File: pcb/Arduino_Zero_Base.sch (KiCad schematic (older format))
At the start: 14 parts, among them U4 SAMD21G18A-A, Y1 32.768kHz

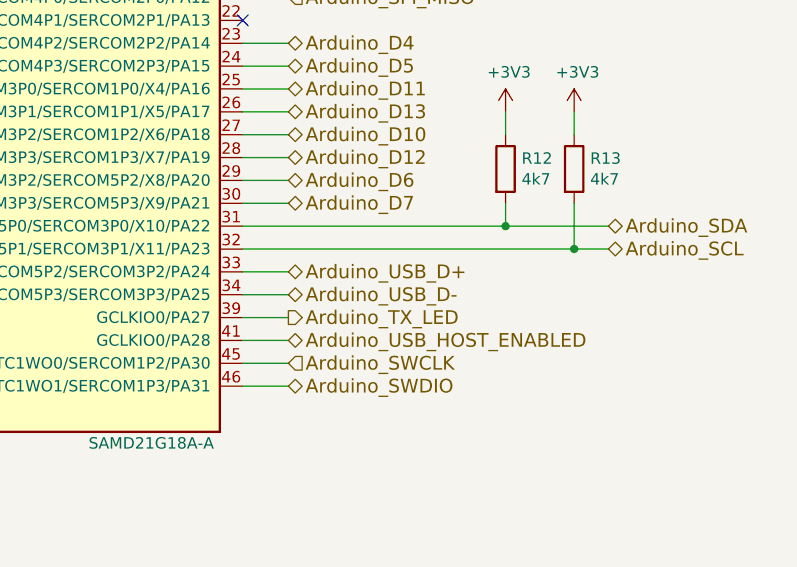
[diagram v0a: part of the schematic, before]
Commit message: Improve pcb routing, add testpoints and etc. The design improves a lot. Still lots to do, but most important design parts should now be drafted almost complete.
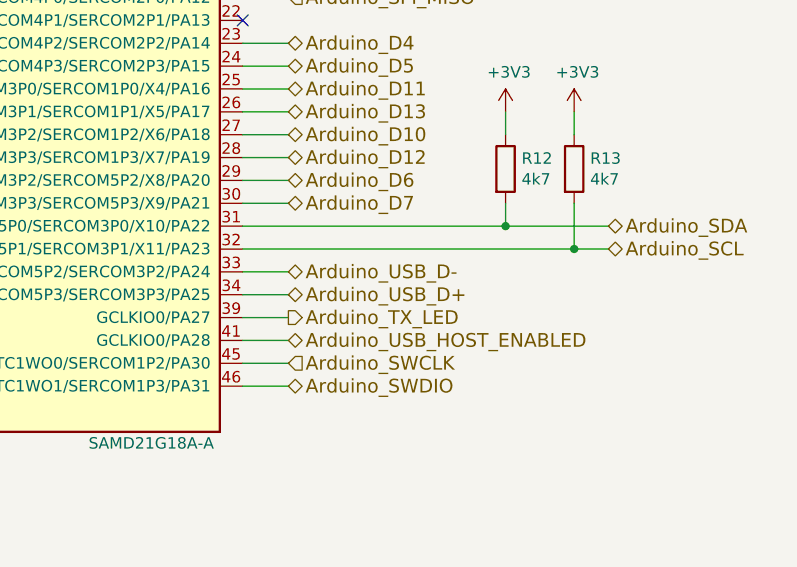
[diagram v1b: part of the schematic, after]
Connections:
- net Arduino_USB_D+: now also U4.34 (USBDP/TC5WO1/SERCOM5P3/SERCOM3P3/PA25); no longer U4.33 (USBDM/TC5WO0/SERCOM5P2/SERCOM3P2/PA24)
- net Arduino_USB_D-: now also U4.33 (USBDM/TC5WO0/SERCOM5P2/SERCOM3P2/PA24); no longer U4.34 (USBDP/TC5WO1/SERCOM5P3/SERCOM3P3/PA25)
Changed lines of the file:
@@
 $EndDescr
 $Comp
-L GND #PWR036
+L GND #PWR045
 U 1 1 5802079F
 P 8800 3350
-F 0 "#PWR036" H 8800 3100 50  0001 C CNN
+F 0 "#PWR045" H 8800 3100 50  0001 C CNN
 F 1 "GND" H 8805 3177 50  0000 C CNN
 F 2 "" H 8800 3350 50  0000 C CNN
@@
 $EndComp
 $Comp
-L GND #PWR037
+L GND #PWR046
 U 1 1 580207D5
 P 9200 3350
-F 0 "#PWR037" H 9200 3100 50  0001 C CNN
+F 0 "#PWR046" H 9200 3100 50  0001 C CNN
 F 1 "GND" H 9205 3177 50  0000 C CNN
 F 2 "" H 9200 3350 50  0000 C CNN
@@
 Connection ~ 8800 2950
 $Comp
-L GND #PWR038
+L GND #PWR047
 U 1 1 58028479
 P 5350 6050
-F 0 "#PWR038" H 5350 5800 50  0001 C CNN
+F 0 "#PWR047" H 5350 5800 50  0001 C CNN
 F 1 "GND" H 5355 5877 50  0000 C CNN
 F 2 "" H 5350 6050 50  0000 C CNN
@@
 $EndComp
 $Comp
-L GND #PWR039
+L GND #PWR048
 U 1 1 5802867C
 P 4950 6050
-F 0 "#PWR039" H 4950 5800 50  0001 C CNN
+F 0 "#PWR048" H 4950 5800 50  0001 C CNN
 F 1 "GND" H 4955 5877 50  0000 C CNN
 F 2 "" H 4950 6050 50  0000 C CNN
@@
 	5250 5950 5250 5850
 $Comp
-L +3V3 #PWR040
+L +3V3 #PWR049
 U 1 1 580289B7
 P 4600 1600
-F 0 "#PWR040" H 4600 1450 50  0001 C CNN
+F 0 "#PWR049" H 4600 1450 50  0001 C CNN
 F 1 "+3V3" H 4615 1773 50  0000 C CNN
 F 2 "" H 4600 1600 50  0000 C CNN
@@
 $EndComp
 $Comp
-L +3V3 #PWR041
+L +3V3 #PWR050
 U 1 1 58028A51
 P 5350 2250
-F 0 "#PWR041" H 5350 2100 50  0001 C CNN
+F 0 "#PWR050" H 5350 2100 50  0001 C CNN
 F 1 "+3V3" H 5365 2423 50  0000 C CNN
 F 2 "" H 5350 2250 50  0000 C CNN
@@
 $EndComp
 $Comp
-L GND #PWR042
+L GND #PWR051
 U 1 1 58028EFC
 P 5550 1950
-F 0 "#PWR042" H 5550 1700 50  0001 C CNN
+F 0 "#PWR051" H 5550 1700 50  0001 C CNN
 F 1 "GND" H 5555 1777 50  0000 C CNN
 F 2 "" H 5550 1950 50  0000 C CNN
@@
 $EndComp
 $Comp
-L GND #PWR043
+L GND #PWR052
 U 1 1 580295A1
 P 4600 2300
-F 0 "#PWR043" H 4600 2050 50  0001 C CNN
+F 0 "#PWR052" H 4600 2050 50  0001 C CNN
 F 1 "GND" H 4605 2127 50  0000 C CNN
 F 2 "" H 4600 2300 50  0000 C CNN
@@
 $EndComp
 $Comp
-L GND #PWR044
+L GND #PWR053
 U 1 1 58029E20
 P 6150 2050
-F 0 "#PWR044" H 6150 1800 50  0001 C CNN
+F 0 "#PWR053" H 6150 1800 50  0001 C CNN
 F 1 "GND" H 6155 1877 50  0000 C CNN
 F 2 "" H 6150 2050 50  0000 C CNN
@@
 $EndComp
 $Comp
-L GND #PWR045
+L GND #PWR054
 U 1 1 58029E5B
 P 7050 2050
-F 0 "#PWR045" H 7050 1800 50  0001 C CNN
+F 0 "#PWR054" H 7050 1800 50  0001 C CNN
 F 1 "GND" H 7055 1877 50  0000 C CNN
 F 2 "" H 7050 2050 50  0000 C CNN
@@
 $EndComp
 $Comp
-L +3V3 #PWR046
+L +3V3 #PWR055
 U 1 1 58029EA6
 P 6150 1650
-F 0 "#PWR046" H 6150 1500 50  0001 C CNN
+F 0 "#PWR055" H 6150 1500 50  0001 C CNN
 F 1 "+3V3" H 6165 1823 50  0000 C CNN
 F 2 "" H 6150 1650 50  0000 C CNN
@@
 $EndComp
 $Comp
-L +3V3 #PWR047
+L +3V3 #PWR056
 U 1 1 58029EE1
 P 7050 1650
-F 0 "#PWR047" H 7050 1500 50  0001 C CNN
+F 0 "#PWR056" H 7050 1500 50  0001 C CNN
 F 1 "+3V3" H 7065 1823 50  0000 C CNN
 F 2 "" H 7050 1650 50  0000 C CNN
@@
 	7450 5150 7650 5150
 Text HLabel 7650 5050 2    60   BiDi ~ 0
+Arduino_USB_D-
+Text HLabel 7650 5150 2    60   BiDi ~ 0
 Arduino_USB_D+
-Text HLabel 7650 5150 2    60   BiDi ~ 0
-Arduino_USB_D-
 Text HLabel 7650 3250 2    60   3State ~ 0
 Arduino_D8
@@
 $EndComp
 $Comp
-L +3V3 #PWR048
+L +3V3 #PWR057
 U 1 1 58034CF0
 P 8600 4350
-F 0 "#PWR048" H 8600 4200 50  0001 C CNN
+F 0 "#PWR057" H 8600 4200 50  0001 C CNN
 F 1 "+3V3" H 8615 4523 50  0000 C CNN
 F 2 "" H 8600 4350 50  0000 C CNN
@@
 $EndComp
 $Comp
-L +3V3 #PWR049
+L +3V3 #PWR058
 U 1 1 58034DB6
 P 8900 4350
-F 0 "#PWR049" H 8900 4200 50  0001 C CNN
+F 0 "#PWR058" H 8900 4200 50  0001 C CNN
 F 1 "+3V3" H 8915 4523 50  0000 C CNN
 F 2 "" H 8900 4350 50  0000 C CNN
@@
 $EndComp
 $Comp
-L GND #PWR050
+L GND #PWR059
 U 1 1 5803933E
 P 7550 2250
-F 0 "#PWR050" H 7550 2000 50  0001 C CNN
+F 0 "#PWR059" H 7550 2000 50  0001 C CNN
 F 1 "GND" H 7555 2077 50  0000 C CNN
 F 2 "" H 7550 2250 50  0000 C CNN
@@
 $EndComp
 $Comp
-L GND #PWR051
+L GND #PWR060
 U 1 1 5807F41A
 P 6600 2050
-F 0 "#PWR051" H 6600 1800 50  0001 C CNN
+F 0 "#PWR060" H 6600 1800 50  0001 C CNN
 F 1 "GND" H 6605 1877 50  0000 C CNN
 F 2 "" H 6600 2050 50  0000 C CNN
@@
 $EndComp
 $Comp
-L +3V3 #PWR052
+L +3V3 #PWR061
 U 1 1 5807F420
 P 6600 1650
-F 0 "#PWR052" H 6600 1500 50  0001 C CNN
+F 0 "#PWR061" H 6600 1500 50  0001 C CNN
 F 1 "+3V3" H 6615 1823 50  0000 C CNN
 F 2 "" H 6600 1650 50  0000 C CNN

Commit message: Add some digikey order informations to components
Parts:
- U4: Digi-Key Minimum Quantity (none) -> 1; Digi-Key Part Number (none) -> ATSAMD21G18A-AUTCT-ND
- Y1: Digi-Key Minimum Quantity (none) -> 1; Digi-Key Part Number (none) -> G83270022CT-ND
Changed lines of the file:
@@
 F 1 "SAMD21G18A-A" H 7050 2500 50  0000 C CNN
 F 2 "Housings_QFP:TQFP-48_7x7mm_Pitch0.5mm" H 5250 3000 50  0001 C CIN
-F 3 "" H 5250 4400 50  0000 C CNN
+F 3 "http://www.atmel.com/Images/Atmel-42181-SAM-D21_Datasheet.pdf" H 5250 4400 50  0001 C CNN
+F 4 "ATSAMD21G18A-AUTCT-ND" H 5250 4150 60  0001 C CNN "Digi-Key Part Number"
+F 5 "1" H 5250 4150 60  0001 C CNN "Digi-Key Minimum Quantity"
 	1    5250 4150
 	1    0    0    -1
@@
 F 1 "32.768kHz" H 9000 3084 50  0000 C CNN
 F 2 "Crystals:Crystal_SMD_G8" H 9000 2950 50  0001 C CNN
-F 3 "" H 9000 2950 50  0000 C CNN
+F 3 "https://media.digikey.com/pdf/Data%20Sheets/Pericom%20PDFs/G83270022_Ver.A.pdf" H 9000 2950 50  0001 C CNN
+F 4 "G83270022CT-ND" H 9000 2950 60  0001 C CNN "Digi-Key Part Number"
+F 5 "1" H 9000 2950 60  0001 C CNN "Digi-Key Minimum Quantity"
 	1    9000 2950
 	1    0    0    -1

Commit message: Add more BOM informations
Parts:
- C10, C11, C12, C13, C14, C9: Digi-Key Minimum Quantity (none) -> 1; Digi-Key Part Number (none) -> 311-1343-1-ND
- C15, C16: Digi-Key Minimum Quantity (none) -> 1; Digi-Key Part Number (none) -> 311-1062-1-ND
- R11: Digi-Key Minimum Quantity (none) -> 5000; Digi-Key Part Number (none) -> 311-330GRTR-ND
- R12, R13: Digi-Key Minimum Quantity (none) -> 5000; Digi-Key Part Number (none) -> 311-4.70KHRTR-ND
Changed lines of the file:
@@
 F 2 "Capacitors_SMD:C_0603" H 9200 3150 50  0001 C CNN
 F 3 "" H 9200 3150 50  0000 C CNN
+F 4 "311-1062-1-ND" H 9200 3150 60  0001 C CNN "Digi-Key Part Number"
+F 5 "1" H 9200 3150 60  0001 C CNN "Digi-Key Minimum Quantity"
 	1    9200 3150
 	-1   0    0    1
@@
 F 2 "Capacitors_SMD:C_0603" H 8800 3150 50  0001 C CNN
 F 3 "" H 8800 3150 50  0000 C CNN
+F 4 "311-1062-1-ND" H 8800 3150 60  0001 C CNN "Digi-Key Part Number"
+F 5 "1" H 8800 3150 60  0001 C CNN "Digi-Key Minimum Quantity"
 	1    8800 3150
 	-1   0    0    1
@@
 F 2 "Capacitors_SMD:C_0603" H 5550 2150 50  0001 C CNN
 F 3 "" H 5550 2150 50  0000 C CNN
+F 4 "311-1343-1-ND" H 5550 2150 60  0001 C CNN "Digi-Key Part Number"
+F 5 "1" H 5550 2150 60  0001 C CNN "Digi-Key Minimum Quantity"
 	1    5550 2150
 	-1   0    0    1
@@
 F 2 "Capacitors_SMD:C_0603" H 4600 2100 50  0001 C CNN
 F 3 "" H 4600 2100 50  0000 C CNN
+F 4 "311-1343-1-ND" H 4600 2100 60  0001 C CNN "Digi-Key Part Number"
+F 5 "1" H 4600 2100 60  0001 C CNN "Digi-Key Minimum Quantity"
 	1    4600 2100
 	-1   0    0    1
@@
 F 2 "Capacitors_SMD:C_0603" H 6150 1850 50  0001 C CNN
 F 3 "" H 6150 1850 50  0000 C CNN
+F 4 "311-1343-1-ND" H 6150 1850 60  0001 C CNN "Digi-Key Part Number"
+F 5 "1" H 6150 1850 60  0001 C CNN "Digi-Key Minimum Quantity"
 	1    6150 1850
 	-1   0    0    1
@@
 F 2 "Capacitors_SMD:C_0603" H 7050 1850 50  0001 C CNN
 F 3 "" H 7050 1850 50  0000 C CNN
+F 4 "311-1343-1-ND" H 7050 1850 60  0001 C CNN "Digi-Key Part Number"
+F 5 "1" H 7050 1850 60  0001 C CNN "Digi-Key Minimum Quantity"
 	1    7050 1850
 	-1   0    0    1
@@
 F 2 "Resistors_SMD:R_0603" V 2730 2650 50  0001 C CNN
 F 3 "" H 2800 2650 50  0000 C CNN
+F 4 "311-330GRTR-ND" H 2800 2650 60  0001 C CNN "Digi-Key Part Number"
+F 5 "5000" H 2800 2650 60  0001 C CNN "Digi-Key Minimum Quantity"
 	1    2800 2650
 	0    -1   -1   0
@@
 F 2 "Resistors_SMD:R_0603" V 8830 4600 50  0001 C CNN
 F 3 "" H 8900 4600 50  0000 C CNN
+F 4 "311-4.70KHRTR-ND" H 8900 4600 60  0001 C CNN "Digi-Key Part Number"
+F 5 "5000" H 8900 4600 60  0001 C CNN "Digi-Key Minimum Quantity"
 	1    8900 4600
 	1    0    0    -1
@@
 F 2 "Resistors_SMD:R_0603" V 8530 4600 50  0001 C CNN
 F 3 "" H 8600 4600 50  0000 C CNN
+F 4 "311-4.70KHRTR-ND" H 8600 4600 60  0001 C CNN "Digi-Key Part Number"
+F 5 "5000" H 8600 4600 60  0001 C CNN "Digi-Key Minimum Quantity"
 	1    8600 4600
 	1    0    0    -1
@@
 F 2 "Capacitors_SMD:C_0603" H 7550 2450 50  0001 C CNN
 F 3 "" H 7550 2450 50  0000 C CNN
+F 4 "311-1343-1-ND" H 7550 2450 60  0001 C CNN "Digi-Key Part Number"
+F 5 "1" H 7550 2450 60  0001 C CNN "Digi-Key Minimum Quantity"
 	1    7550 2450
 	-1   0    0    1
@@
 F 2 "Capacitors_SMD:C_0603" H 6600 1850 50  0001 C CNN
 F 3 "" H 6600 1850 50  0000 C CNN
+F 4 "311-1343-1-ND" H 6600 1850 60  0001 C CNN "Digi-Key Part Number"
+F 5 "1" H 6600 1850 60  0001 C CNN "Digi-Key Minimum Quantity"
 	1    6600 1850
 	-1   0    0    1

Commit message: Improve BOM
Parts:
- L1: value INDUCTOR_Small -> FERRIT_BEAD; Digi-Key Minimum Quantity (none) -> 1; Digi-Key Part Number (none) -> MH1608-471YCT-ND
- R11: Digi-Key Minimum Quantity 5000 -> 1; Digi-Key Part Number 311-330GRTR-ND -> 311-330GRCT-ND
- R12, R13: Digi-Key Minimum Quantity 5000 -> 1; Digi-Key Part Number 311-4.70KHRTR-ND -> 311-4.70KHRCT-ND
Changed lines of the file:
@@
 P 4600 1800
 F 0 "L1" H 4648 1846 50  0000 L CNN
-F 1 "INDUCTOR_Small" H 4648 1755 50  0000 L CNN
+F 1 "FERRIT_BEAD" H 4648 1755 50  0000 L CNN
 F 2 "Resistors_SMD:R_0603" H 4600 1800 50  0001 C CNN
-F 3 "" H 4600 1800 50  0000 C CNN
+F 3 "http://www.bourns.com/docs/Product-Datasheets/mh.pdf" H 4600 1800 50  0001 C CNN
+F 4 "MH1608-471YCT-ND" H 4600 1800 60  0001 C CNN "Digi-Key Part Number"
+F 5 "1" H 4600 1800 60  0001 C CNN "Digi-Key Minimum Quantity"
 	1    4600 1800
 	1    0    0    -1
@@
 F 2 "Resistors_SMD:R_0603" V 2730 2650 50  0001 C CNN
 F 3 "" H 2800 2650 50  0000 C CNN
-F 4 "311-330GRTR-ND" H 2800 2650 60  0001 C CNN "Digi-Key Part Number"
-F 5 "5000" H 2800 2650 60  0001 C CNN "Digi-Key Minimum Quantity"
+F 4 "311-330GRCT-ND" H 2800 2650 60  0001 C CNN "Digi-Key Part Number"
+F 5 "1" H 2800 2650 60  0001 C CNN "Digi-Key Minimum Quantity"
 	1    2800 2650
 	0    -1   -1   0
@@
 F 2 "Resistors_SMD:R_0603" V 8830 4600 50  0001 C CNN
 F 3 "" H 8900 4600 50  0000 C CNN
-F 4 "311-4.70KHRTR-ND" H 8900 4600 60  0001 C CNN "Digi-Key Part Number"
-F 5 "5000" H 8900 4600 60  0001 C CNN "Digi-Key Minimum Quantity"
+F 4 "311-4.70KHRCT-ND" H 8900 4600 60  0001 C CNN "Digi-Key Part Number"
+F 5 "1" H 8900 4600 60  0001 C CNN "Digi-Key Minimum Quantity"
 	1    8900 4600
 	1    0    0    -1
@@
 F 2 "Resistors_SMD:R_0603" V 8530 4600 50  0001 C CNN
 F 3 "" H 8600 4600 50  0000 C CNN
-F 4 "311-4.70KHRTR-ND" H 8600 4600 60  0001 C CNN "Digi-Key Part Number"
-F 5 "5000" H 8600 4600 60  0001 C CNN "Digi-Key Minimum Quantity"
+F 4 "311-4.70KHRCT-ND" H 8600 4600 60  0001 C CNN "Digi-Key Part Number"
+F 5 "1" H 8600 4600 60  0001 C CNN "Digi-Key Minimum Quantity"
 	1    8600 4600
 	1    0    0    -1

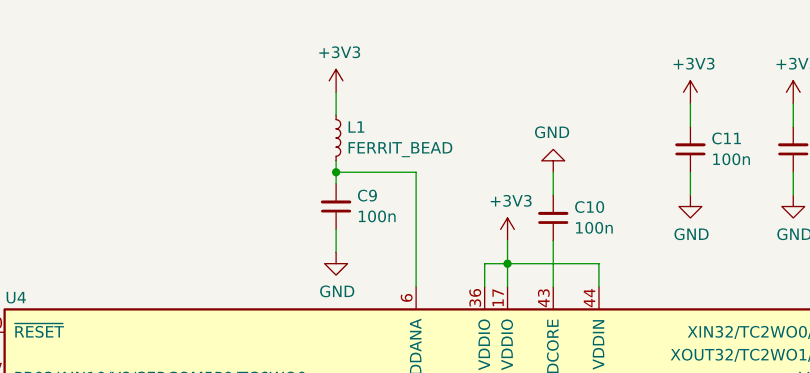
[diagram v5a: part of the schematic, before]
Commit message: Use new library symbols
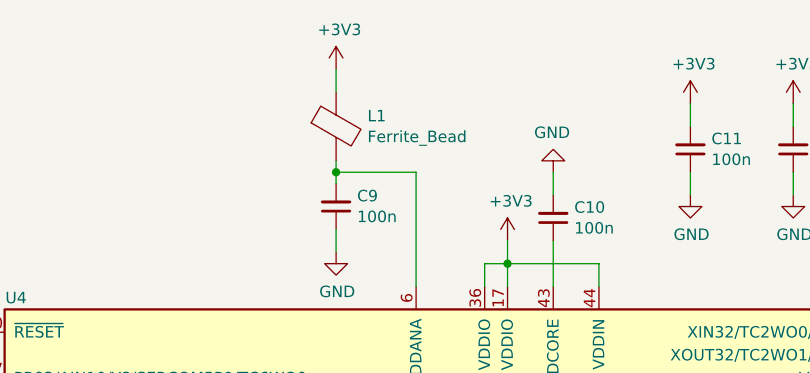
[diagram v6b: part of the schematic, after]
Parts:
- removed L1: FERRIT_BEAD, Resistors_SMD:R_0603, symbol INDUCTOR_Small
- added L1: Ferrite_Bead, Resistors_SMD:R_0603, symbol Ferrite_Bead
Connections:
- net +3V3: now also L1.1
- net at C9.2, U4.6 (VDDANA): now also L1.2
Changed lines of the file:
@@
 L +3V3 #PWR050
 U 1 1 580289B7
-P 4600 1600
-F 0 "#PWR050" H 4600 1450 50  0001 C CNN
-F 1 "+3V3" H 4615 1773 50  0000 C CNN
-F 2 "" H 4600 1600 50  0000 C CNN
-F 3 "" H 4600 1600 50  0000 C CNN
-	1    4600 1600
+P 4600 1500
+F 0 "#PWR050" H 4600 1350 50  0001 C CNN
+F 1 "+3V3" H 4615 1673 50  0000 C CNN
+F 2 "" H 4600 1500 50  0000 C CNN
+F 3 "" H 4600 1500 50  0000 C CNN
+	1    4600 1500
 	1    0    0    -1
 $EndComp
@@
 $EndComp
 $Comp
-L INDUCTOR_Small L1
-U 1 1 580294AF
-P 4600 1800
-F 0 "L1" H 4648 1846 50  0000 L CNN
-F 1 "FERRIT_BEAD" H 4648 1755 50  0000 L CNN
-F 2 "Resistors_SMD:R_0603" H 4600 1800 50  0001 C CNN
-F 3 "http://www.bourns.com/docs/Product-Datasheets/mh.pdf" H 4600 1800 50  0001 C CNN
-F 4 "MH1608-471YCT-ND" H 4600 1800 60  0001 C CNN "Digi-Key Part Number"
-F 5 "1" H 4600 1800 60  0001 C CNN "Digi-Key Minimum Quantity"
-	1    4600 1800
-	1    0    0    -1
-$EndComp
-$Comp
 L C_Small C9
 U 1 1 58029539
@@
 Connection ~ 4600 1950
 Wire Wire Line
-	4600 1600 4600 1700
+	4600 1500 4600 1600
 $Comp
 L C_Small C11
@@
 Wire Wire Line
 	6600 1950 6600 2050
+$Comp
+L Ferrite_Bead L1
+U 1 1 582EB9E4
+P 4600 1750
+F 0 "L1" H 4737 1796 50  0000 L CNN
+F 1 "Ferrite_Bead" H 4737 1705 50  0000 L CNN
+F 2 "Resistors_SMD:R_0603" H 4737 1659 50  0001 L CNN
+F 3 "http://www.bourns.com/docs/Product-Datasheets/mh.pdf" H 4737 1659 50  0001 L CNN
+F 4 "MH1608-471YCT-ND" H 4600 1750 60  0001 C CNN "Digi-Key Part Number"
+F 5 "1" H 4600 1750 60  0001 C CNN "Digi-Key Minimum Quantity"
+	1    4600 1750
+	1    0    0    -1
+$EndComp
 $EndSCHEMATC

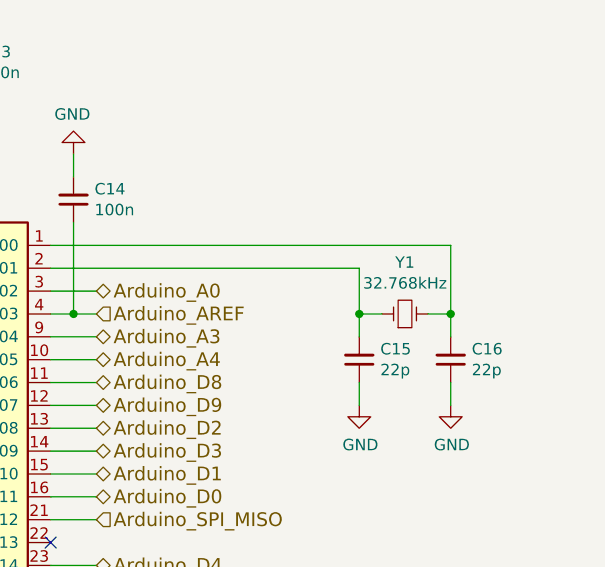
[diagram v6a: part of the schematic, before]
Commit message: Improve layout and add voltage sensing circuit to layout
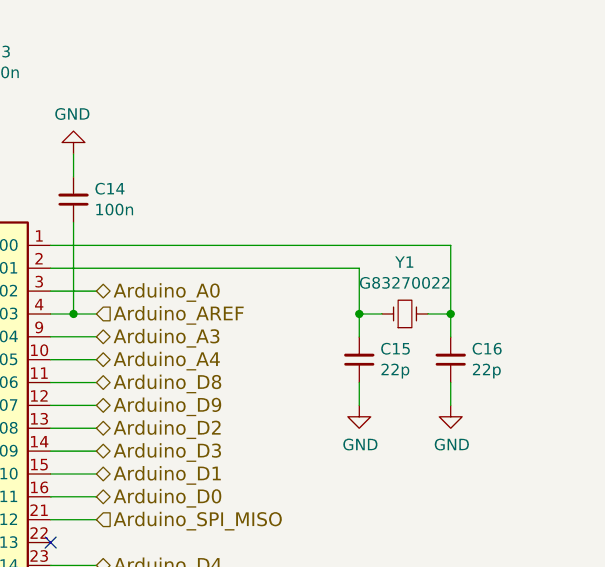
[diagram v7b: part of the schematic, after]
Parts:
- Y1: value 32.768kHz -> G83270022
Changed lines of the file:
@@
 $EndDescr
 $Comp
-L GND #PWR046
+L GND #PWR049
 U 1 1 5802079F
 P 8800 3350
-F 0 "#PWR046" H 8800 3100 50  0001 C CNN
+F 0 "#PWR049" H 8800 3100 50  0001 C CNN
 F 1 "GND" H 8805 3177 50  0000 C CNN
 F 2 "" H 8800 3350 50  0000 C CNN
@@
 $EndComp
 $Comp
-L GND #PWR047
+L GND #PWR050
 U 1 1 580207D5
 P 9200 3350
-F 0 "#PWR047" H 9200 3100 50  0001 C CNN
+F 0 "#PWR050" H 9200 3100 50  0001 C CNN
 F 1 "GND" H 9205 3177 50  0000 C CNN
 F 2 "" H 9200 3350 50  0000 C CNN
@@
 P 9000 2950
 F 0 "Y1" H 9000 3175 50  0000 C CNN
-F 1 "32.768kHz" H 9000 3084 50  0000 C CNN
+F 1 "G83270022" H 9000 3084 50  0000 C CNN
 F 2 "Crystals:Crystal_SMD_G8" H 9000 2950 50  0001 C CNN
 F 3 "https://media.digikey.com/pdf/Data%20Sheets/Pericom%20PDFs/G83270022_Ver.A.pdf" H 9000 2950 50  0001 C CNN
@@
 Connection ~ 8800 2950
 $Comp
-L GND #PWR048
+L GND #PWR051
 U 1 1 58028479
 P 5350 6050
-F 0 "#PWR048" H 5350 5800 50  0001 C CNN
+F 0 "#PWR051" H 5350 5800 50  0001 C CNN
 F 1 "GND" H 5355 5877 50  0000 C CNN
 F 2 "" H 5350 6050 50  0000 C CNN
@@
 $EndComp
 $Comp
-L GND #PWR049
+L GND #PWR052
 U 1 1 5802867C
 P 4950 6050
-F 0 "#PWR049" H 4950 5800 50  0001 C CNN
+F 0 "#PWR052" H 4950 5800 50  0001 C CNN
 F 1 "GND" H 4955 5877 50  0000 C CNN
 F 2 "" H 4950 6050 50  0000 C CNN
@@
 	5250 5950 5250 5850
 $Comp
-L +3V3 #PWR050
+L +3V3 #PWR053
 U 1 1 580289B7
 P 4600 1500
-F 0 "#PWR050" H 4600 1350 50  0001 C CNN
+F 0 "#PWR053" H 4600 1350 50  0001 C CNN
 F 1 "+3V3" H 4615 1673 50  0000 C CNN
 F 2 "" H 4600 1500 50  0000 C CNN
@@
 $EndComp
 $Comp
-L +3V3 #PWR051
+L +3V3 #PWR054
 U 1 1 58028A51
 P 5350 2250
-F 0 "#PWR051" H 5350 2100 50  0001 C CNN
+F 0 "#PWR054" H 5350 2100 50  0001 C CNN
 F 1 "+3V3" H 5365 2423 50  0000 C CNN
 F 2 "" H 5350 2250 50  0000 C CNN
@@
 $EndComp
 $Comp
-L GND #PWR052
+L GND #PWR055
 U 1 1 58028EFC
 P 5550 1950
-F 0 "#PWR052" H 5550 1700 50  0001 C CNN
+F 0 "#PWR055" H 5550 1700 50  0001 C CNN
 F 1 "GND" H 5555 1777 50  0000 C CNN
 F 2 "" H 5550 1950 50  0000 C CNN
@@
 $EndComp
 $Comp
-L GND #PWR053
+L GND #PWR056
 U 1 1 580295A1
 P 4600 2300
-F 0 "#PWR053" H 4600 2050 50  0001 C CNN
+F 0 "#PWR056" H 4600 2050 50  0001 C CNN
 F 1 "GND" H 4605 2127 50  0000 C CNN
 F 2 "" H 4600 2300 50  0000 C CNN
@@
 $EndComp
 $Comp
-L GND #PWR054
+L GND #PWR057
 U 1 1 58029E20
 P 6150 2050
-F 0 "#PWR054" H 6150 1800 50  0001 C CNN
+F 0 "#PWR057" H 6150 1800 50  0001 C CNN
 F 1 "GND" H 6155 1877 50  0000 C CNN
 F 2 "" H 6150 2050 50  0000 C CNN
@@
 $EndComp
 $Comp
-L GND #PWR055
+L GND #PWR058
 U 1 1 58029E5B
 P 7050 2050
-F 0 "#PWR055" H 7050 1800 50  0001 C CNN
+F 0 "#PWR058" H 7050 1800 50  0001 C CNN
 F 1 "GND" H 7055 1877 50  0000 C CNN
 F 2 "" H 7050 2050 50  0000 C CNN
@@
 $EndComp
 $Comp
-L +3V3 #PWR056
+L +3V3 #PWR059
 U 1 1 58029EA6
 P 6150 1650
-F 0 "#PWR056" H 6150 1500 50  0001 C CNN
+F 0 "#PWR059" H 6150 1500 50  0001 C CNN
 F 1 "+3V3" H 6165 1823 50  0000 C CNN
 F 2 "" H 6150 1650 50  0000 C CNN
@@
 $EndComp
 $Comp
-L +3V3 #PWR057
+L +3V3 #PWR060
 U 1 1 58029EE1
 P 7050 1650
-F 0 "#PWR057" H 7050 1500 50  0001 C CNN
+F 0 "#PWR060" H 7050 1500 50  0001 C CNN
 F 1 "+3V3" H 7065 1823 50  0000 C CNN
 F 2 "" H 7050 1650 50  0000 C CNN
@@
 $EndComp
 $Comp
-L +3V3 #PWR058
+L +3V3 #PWR061
 U 1 1 58034CF0
 P 8600 4350
-F 0 "#PWR058" H 8600 4200 50  0001 C CNN
+F 0 "#PWR061" H 8600 4200 50  0001 C CNN
 F 1 "+3V3" H 8615 4523 50  0000 C CNN
 F 2 "" H 8600 4350 50  0000 C CNN
@@
 $EndComp
 $Comp
-L +3V3 #PWR059
+L +3V3 #PWR062
 U 1 1 58034DB6
 P 8900 4350
-F 0 "#PWR059" H 8900 4200 50  0001 C CNN
+F 0 "#PWR062" H 8900 4200 50  0001 C CNN
 F 1 "+3V3" H 8915 4523 50  0000 C CNN
 F 2 "" H 8900 4350 50  0000 C CNN
@@
 $EndComp
 $Comp
-L GND #PWR060
+L GND #PWR063
 U 1 1 5803933E
 P 7550 2250
-F 0 "#PWR060" H 7550 2000 50  0001 C CNN
+F 0 "#PWR063" H 7550 2000 50  0001 C CNN
 F 1 "GND" H 7555 2077 50  0000 C CNN
 F 2 "" H 7550 2250 50  0000 C CNN
@@
 $EndComp
 $Comp
-L GND #PWR061
+L GND #PWR064
 U 1 1 5807F41A
 P 6600 2050
-F 0 "#PWR061" H 6600 1800 50  0001 C CNN
+F 0 "#PWR064" H 6600 1800 50  0001 C CNN
 F 1 "GND" H 6605 1877 50  0000 C CNN
 F 2 "" H 6600 2050 50  0000 C CNN
@@
 $EndComp
 $Comp
-L +3V3 #PWR062
+L +3V3 #PWR065
 U 1 1 5807F420
 P 6600 1650
-F 0 "#PWR062" H 6600 1500 50  0001 C CNN
+F 0 "#PWR065" H 6600 1500 50  0001 C CNN
 F 1 "+3V3" H 6615 1823 50  0000 C CNN
 F 2 "" H 6600 1650 50  0000 C CNN
